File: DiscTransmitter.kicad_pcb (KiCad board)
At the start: 2 copper layers, 53.4 x 19.7 mm, 41 parts, among them J1 Conn_01x01_Male, J2 Conn_01x01_Male, J3 Conn_01x04_Male, J4 Conn_01x01_Male, U1 SNx4HC595_8b_Shift_Reg, U2 4-DigitSevenSegment, U3 SNx4HC595_8b_Shift_Reg, U4 SNx4HC595_8b_Shift_Reg, U5 SNx4HC595_8b_Shift_Reg

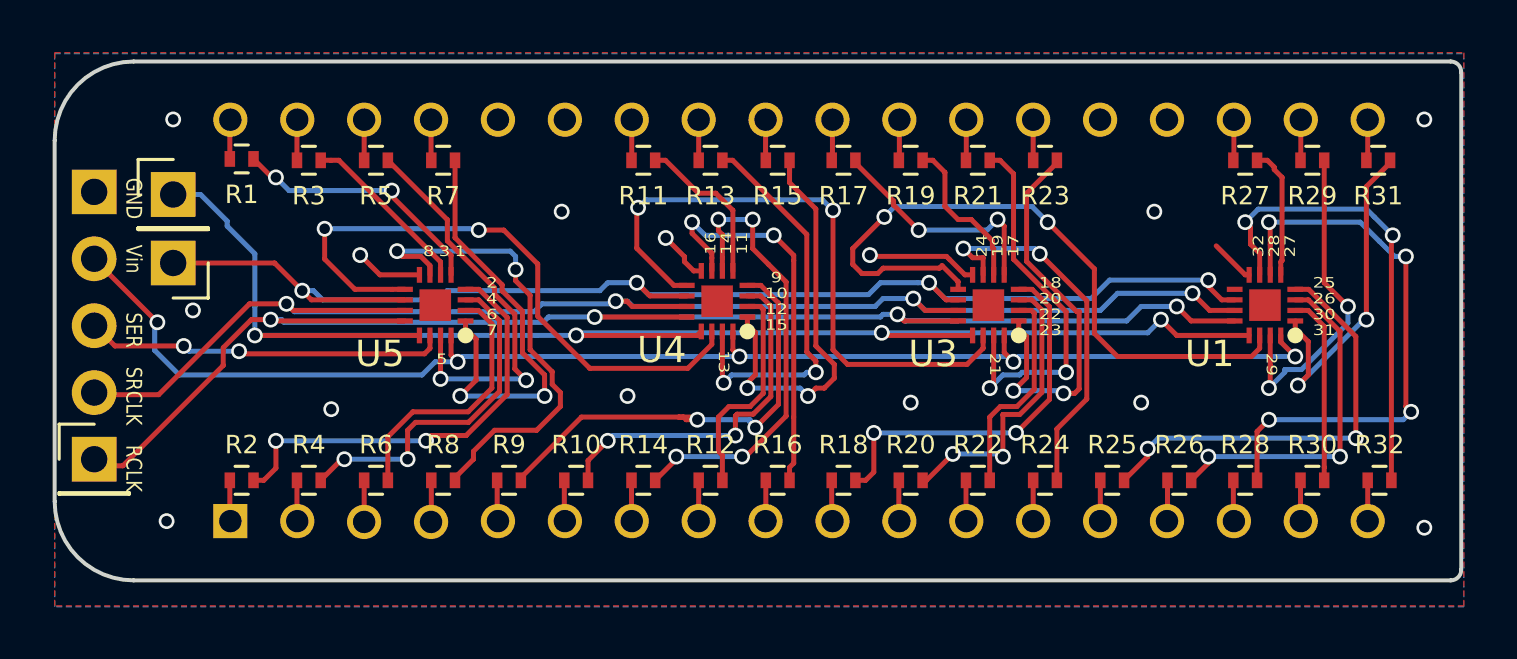
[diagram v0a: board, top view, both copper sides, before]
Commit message: Fixed pads on RFM footprint
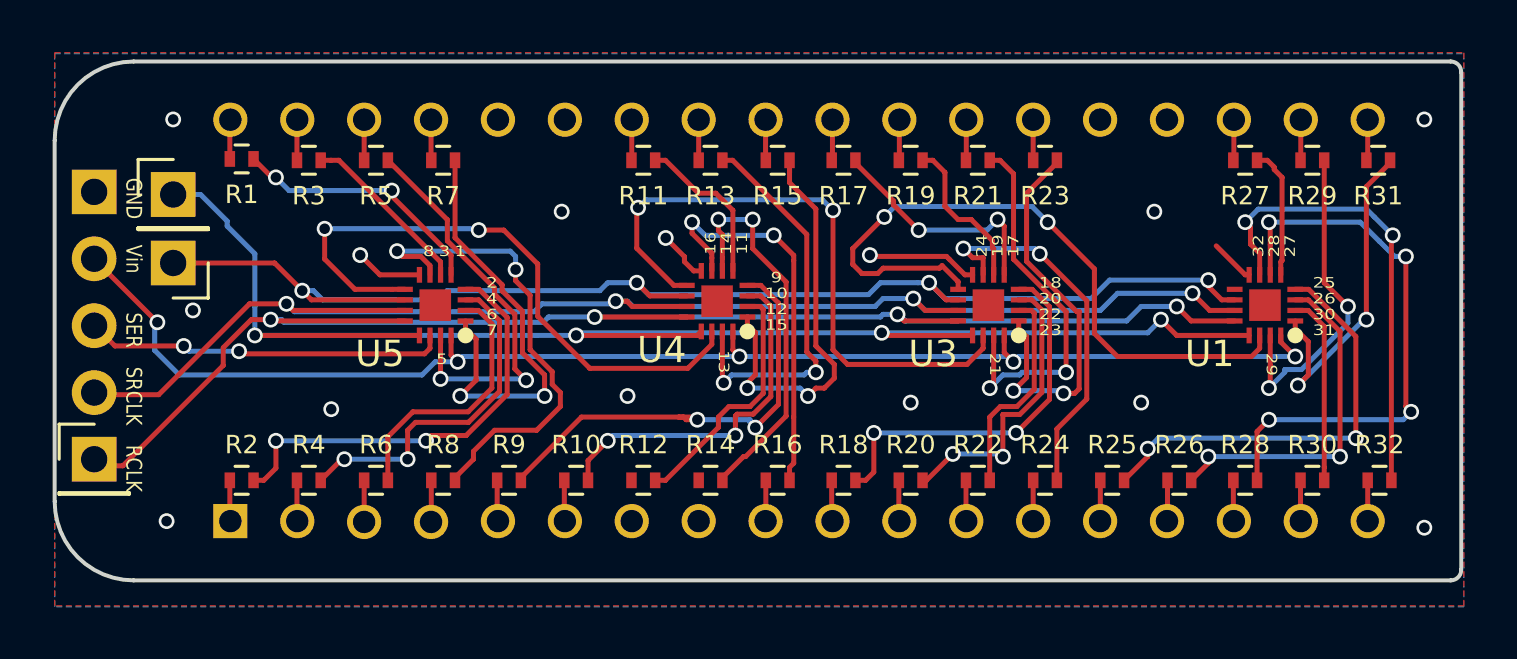
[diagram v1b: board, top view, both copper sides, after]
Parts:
- U2: footprint my_foot_prints:FourDigitSevenSegmentDisplay -> my_foot_prints:TwoDigDisplayX2
- moved R12 2.55 mm to (120.3, 97.2)
- moved R14 2.55 mm to (122.9, 97.2)
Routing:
- net Net-(R14-Pad2): track 17.3 -> 14.8 mm, vias 4 -> 2
- net Net-(R14-Pad1): track 1.55 -> 0.00 mm
- net Net-(R12-Pad1): track 1.55 -> 0.01 mm
- net Net-(R12-Pad2): track 8.37 -> 9.53 mm

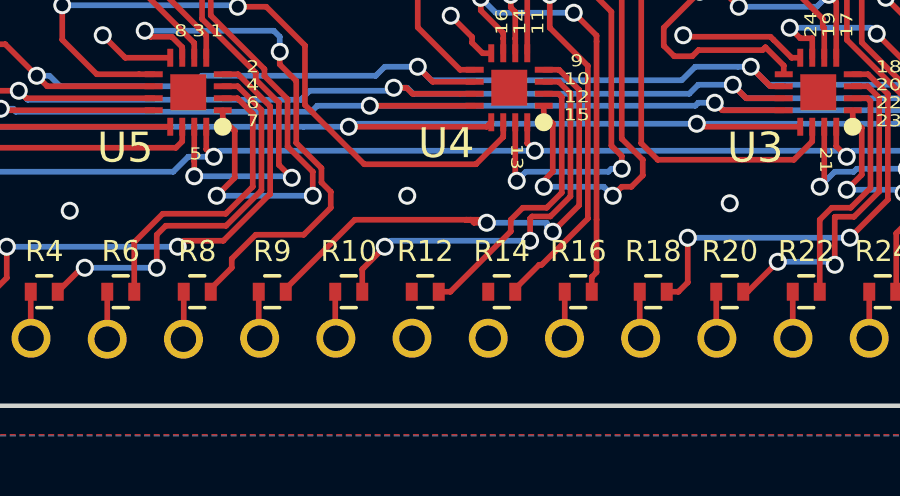
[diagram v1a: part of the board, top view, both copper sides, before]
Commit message: Added two traces I previously forgot.
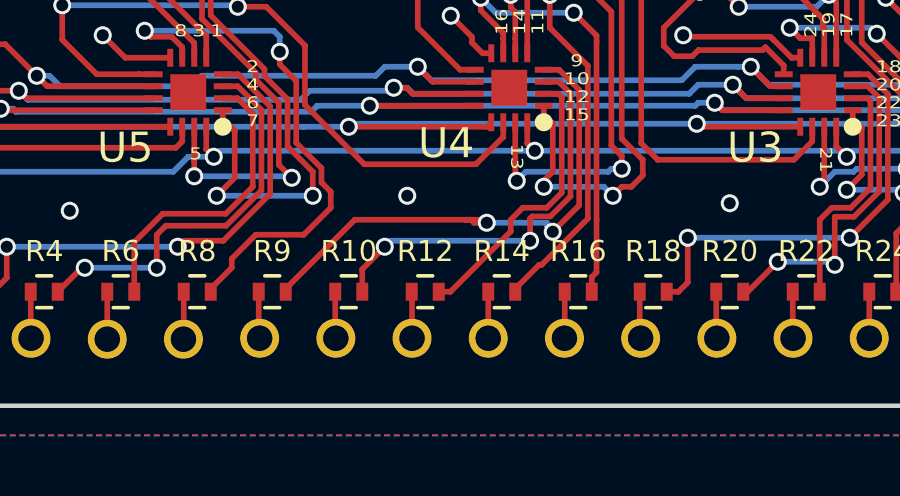
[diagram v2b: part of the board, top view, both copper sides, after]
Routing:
- net Net-(R12-Pad1): track 0.01 -> 1.57 mm
- net Net-(R14-Pad1): track 0.00 -> 1.55 mm
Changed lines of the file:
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@@
     (thickness 1.6)
     (drawings 54)
-    (tracks 660)
+    (tracks 663)
     (zones 0)
     (modules 41)
@@
   (segment (start 119.91 83.51) (end 119.91 85.04) (width 0.19) (layer F.Cu) (net 22))
   (segment (start 119.91 85.04) (end 119.9 85.05) (width 0.19) (layer F.Cu) (net 22))
+  (segment (start 119.9 98.74) (end 119.91 98.75) (width 0.19) (layer F.Cu) (net 23))
+  (segment (start 119.91 97.21) (end 119.9 97.2) (width 0.19) (layer F.Cu) (net 23))
+  (segment (start 119.91 98.75) (end 119.91 97.21) (width 0.19) (layer F.Cu) (net 23))
   (segment (start 124.3 90.6) (end 124.79 90.6) (width 0.19) (layer F.Cu) (net 24))
   (segment (start 124.9 90.71) (end 124.9 93.9) (width 0.19) (layer F.Cu) (net 24))
@@
   (segment (start 124.4 94.4) (end 123.6 94.4) (width 0.19) (layer F.Cu) (net 24))
   (segment (start 123.6 94.4) (end 123.2 94.8) (width 0.19) (layer F.Cu) (net 24))
+  (segment (start 121.19 97.2) (end 120.8 97.2) (width 0.19) (layer F.Cu) (net 24))
+  (segment (start 123.2 95.19) (end 121.19 97.2) (width 0.19) (layer F.Cu) (net 24))
+  (segment (start 123.2 94.8) (end 123.2 95.19) (width 0.19) (layer F.Cu) (net 24))
   (segment (start 123.4 93.5) (end 123.699999 93.200001) (width 0.19) (layer B.Cu) (net 25))
   (segment (start 126.455036 93.200001) (end 126.555037 93.1) (width 0.19) (layer B.Cu) (net 25))
@@
   (segment (start 126.555037 87.865037) (end 123.74 85.05) (width 0.19) (layer F.Cu) (net 25))
   (segment (start 122.45 83.51) (end 122.45 85.05) (width 0.19) (layer F.Cu) (net 26))
-  (segment (start 119.9 98.74) (end 119.91 98.75) (width 0.19) (layer F.Cu) (net 23))
-  (segment (start 121.19 97.2) (end 120.8 97.2) (width 0.19) (layer F.Cu) (net 24))
-  (segment (start 123.2 95.19) (end 121.19 97.2) (width 0.19) (layer F.Cu) (net 24))
-  (segment (start 123.2 94.8) (end 123.2 95.19) (width 0.19) (layer F.Cu) (net 24))
+  (segment (start 122.45 97.2) (end 122.45 98.75) (width 0.19) (layer F.Cu) (net 27))
   (segment (start 123.2 87.3) (end 123.2 87.724264) (width 0.19) (layer F.Cu) (net 28))
   (segment (start 123.2 87.724264) (end 123.35 87.874264) (width 0.19) (layer F.Cu) (net 28))
